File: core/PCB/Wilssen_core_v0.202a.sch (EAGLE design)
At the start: 38 parts, among them Q1 8Mhz, T1 BC849, U1 MAX1555, U2 3.3V, U3 ATMEGA168/ATMEGA328, X1 USBSMD

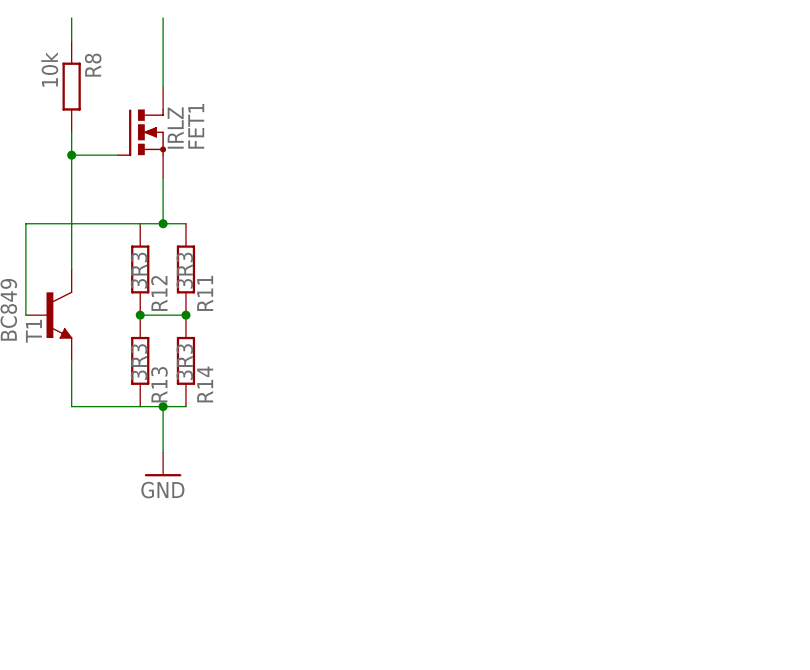
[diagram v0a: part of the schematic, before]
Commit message: CCS2 added
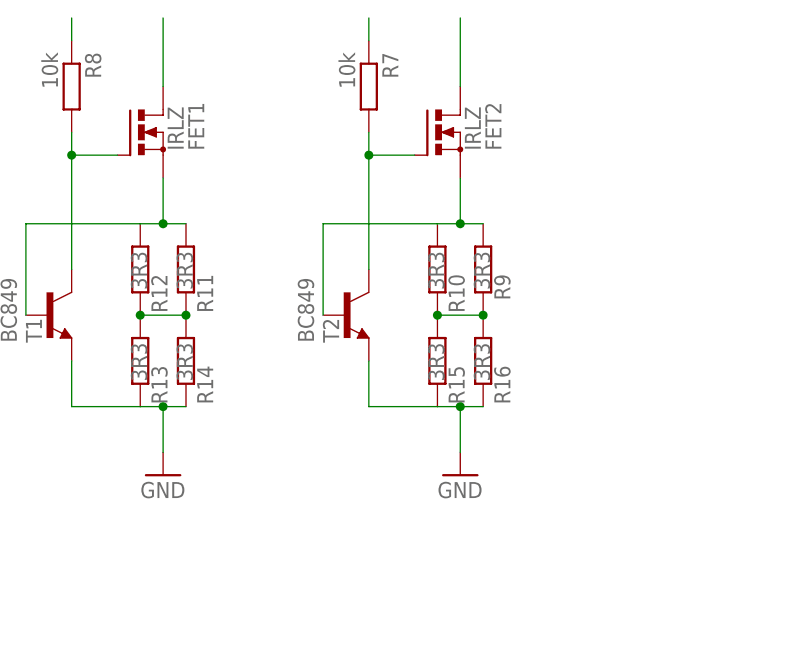
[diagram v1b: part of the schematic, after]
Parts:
- added FET2: IRLZ, transistor-power:PMOSFET_NTO220BV
- added R10, R15, R16, R9: 3R3, resistor:R-EU_R1206
- added R7: 10k, resistor:R-EU_R0805
- added T2: BC849, transistor:BC849
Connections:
- new net GATE2: FET2.G, R7.2, T2.C
- new net LED-OUT_G: FET2.D
- new net NS$2: R10.2, R15.1, R16.1, R9.2
- new net SRC2: FET2.S, R10.1, R9.1, T2.B
- net D5_LED-G: now also R7.1
- net GND: now also R15.2, R16.2, T2.E
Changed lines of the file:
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@@
 <part name="R14" library="resistor" deviceset="R-EU_" device="R1206" value="3R3"/>
 <part name="FRAME1" library="frames" deviceset="DINA5_L" device=""/>
+<part name="GND15" library="supply1" deviceset="GND" device=""/>
+<part name="FET2" library="transistor-power" deviceset="PMOSFET_N" device="TO220BV" value="IRLZ"/>
+<part name="R7" library="resistor" deviceset="R-EU_" device="R0805" value="10k"/>
+<part name="T2" library="transistor" deviceset="BC849" device=""/>
+<part name="R9" library="resistor" deviceset="R-EU_" device="R1206" value="3R3"/>
+<part name="R10" library="resistor" deviceset="R-EU_" device="R1206" value="3R3"/>
+<part name="R15" library="resistor" deviceset="R-EU_" device="R1206" value="3R3"/>
+<part name="R16" library="resistor" deviceset="R-EU_" device="R1206" value="3R3"/>
 </parts>
 <sheets>
@@
 </instance>
 <instance part="FRAME1" gate="G$1" x="-5.08" y="261.62"/>
+<instance part="GND15" gate="1" x="78.74" y="307.34"/>
+<instance part="FET2" gate="G$1" x="76.2" y="345.44" smashed="yes">
+<attribute name="NAME" x="83.312" y="343.408" size="1.778" layer="95" rot="R90"/>
+<attribute name="VALUE" x="81.026" y="343.408" size="1.778" layer="96" rot="R90"/>
+</instance>
+<instance part="R7" gate="G$1" x="68.58" y="350.52" rot="R270"/>
+<instance part="T2" gate="G$1" x="66.04" y="325.12" smashed="yes">
+<attribute name="NAME" x="65.278" y="322.072" size="1.778" layer="95" rot="R90"/>
+<attribute name="VALUE" x="62.484" y="322.072" size="1.778" layer="96" rot="R90"/>
+</instance>
+<instance part="R9" gate="G$1" x="81.28" y="330.2" smashed="yes" rot="R270">
+<attribute name="NAME" x="82.5246" y="329.692" size="1.778" layer="95" rot="R270"/>
+<attribute name="VALUE" x="80.264" y="332.232" size="1.778" layer="96" rot="R270"/>
+</instance>
+<instance part="R10" gate="G$1" x="76.2" y="330.2" smashed="yes" rot="R270">
+<attribute name="NAME" x="77.4446" y="329.692" size="1.778" layer="95" rot="R270"/>
+<attribute name="VALUE" x="75.184" y="332.232" size="1.778" layer="96" rot="R270"/>
+</instance>
+<instance part="R15" gate="G$1" x="76.2" y="320.04" smashed="yes" rot="R270">
+<attribute name="NAME" x="77.4446" y="319.532" size="1.778" layer="95" rot="R270"/>
+<attribute name="VALUE" x="75.184" y="322.072" size="1.778" layer="96" rot="R270"/>
+</instance>
+<instance part="R16" gate="G$1" x="81.28" y="320.04" smashed="yes" rot="R270">
+<attribute name="NAME" x="82.5246" y="319.532" size="1.778" layer="95" rot="R270"/>
+<attribute name="VALUE" x="80.264" y="322.072" size="1.778" layer="96" rot="R270"/>
+</instance>
 </instances>
 <busses>
@@
 <junction x="45.72" y="314.96"/>
 <wire x1="45.72" y1="314.96" x2="43.18" y2="314.96" width="0.1524" layer="91"/>
+</segment>
+<segment>
+<wire x1="68.58" y1="320.04" x2="68.58" y2="314.96" width="0.1524" layer="91"/>
+<wire x1="68.58" y1="314.96" x2="76.2" y2="314.96" width="0.1524" layer="91"/>
+<wire x1="78.74" y1="314.96" x2="78.74" y2="309.88" width="0.1524" layer="91"/>
+<wire x1="81.28" y1="314.96" x2="78.74" y2="314.96" width="0.1524" layer="91"/>
+<pinref part="T2" gate="G$1" pin="E"/>
+<pinref part="GND15" gate="1" pin="GND"/>
+<pinref part="R16" gate="G$1" pin="2"/>
+<pinref part="R15" gate="G$1" pin="2"/>
+<junction x="78.74" y="314.96"/>
+<wire x1="78.74" y1="314.96" x2="76.2" y2="314.96" width="0.1524" layer="91"/>
 </segment>
 </net>
@@
 <pinref part="ATMEGA168/ATMEGA328" gate="G$1" pin="PD5(T1)"/>
 </segment>
+<segment>
+<pinref part="R7" gate="G$1" pin="1"/>
+<wire x1="68.58" y1="355.6" x2="68.58" y2="358.14" width="0.1524" layer="91"/>
+</segment>
 </net>
 <net name="D6_LED-B" class="0">
@@
 </segment>
 </net>
+<net name="GATE2" class="0">
+<segment>
+<wire x1="68.58" y1="330.2" x2="68.58" y2="342.9" width="0.1524" layer="91"/>
+<pinref part="R7" gate="G$1" pin="2"/>
+<pinref part="T2" gate="G$1" pin="C"/>
+<pinref part="FET2" gate="G$1" pin="G"/>
+<wire x1="68.58" y1="342.9" x2="68.58" y2="345.44" width="0.1524" layer="91"/>
+<wire x1="73.66" y1="342.9" x2="68.58" y2="342.9" width="0.1524" layer="91"/>
+<junction x="68.58" y="342.9"/>
+</segment>
+</net>
+<net name="SRC2" class="0">
+<segment>
+<wire x1="63.5" y1="325.12" x2="63.5" y2="335.28" width="0.1524" layer="91"/>
+<wire x1="63.5" y1="335.28" x2="76.2" y2="335.28" width="0.1524" layer="91"/>
+<wire x1="81.28" y1="335.28" x2="78.74" y2="335.28" width="0.1524" layer="91"/>
+<wire x1="76.2" y1="335.28" x2="78.74" y2="335.28" width="0.1524" layer="91"/>
+<wire x1="78.74" y1="335.28" x2="78.74" y2="340.36" width="0.1524" layer="91"/>
+<pinref part="FET2" gate="G$1" pin="S"/>
+<pinref part="T2" gate="G$1" pin="B"/>
+<pinref part="R9" gate="G$1" pin="1"/>
+<pinref part="R10" gate="G$1" pin="1"/>
+<junction x="78.74" y="335.28"/>
+</segment>
+</net>
+<net name="NS$2" class="0">
+<segment>
+<wire x1="81.28" y1="325.12" x2="76.2" y2="325.12" width="0.1524" layer="91"/>
+<pinref part="R9" gate="G$1" pin="2"/>
+<pinref part="R16" gate="G$1" pin="1"/>
+<pinref part="R10" gate="G$1" pin="2"/>
+<pinref part="R15" gate="G$1" pin="1"/>
+<junction x="76.2" y="325.12"/>
+<junction x="81.28" y="325.12"/>
+</segment>
+</net>
+<net name="LED-OUT_G" class="0">
+<segment>
+<wire x1="78.74" y1="350.52" x2="78.74" y2="358.14" width="0.1524" layer="91"/>
+<pinref part="FET2" gate="G$1" pin="D"/>
+</segment>
+</net>
